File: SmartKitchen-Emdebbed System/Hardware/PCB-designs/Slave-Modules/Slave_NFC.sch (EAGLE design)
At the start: 29 parts, among them IC1 PCF8574T, IC2 7805DT, IC3 PCF8574T, IC4 74AHC1G126DBV, J1 RJ11-2L-B, J2 RJ11-2L-B, Q1 SPB80P06P, Q2 SPB80P06P, Q3 SPB80P06P

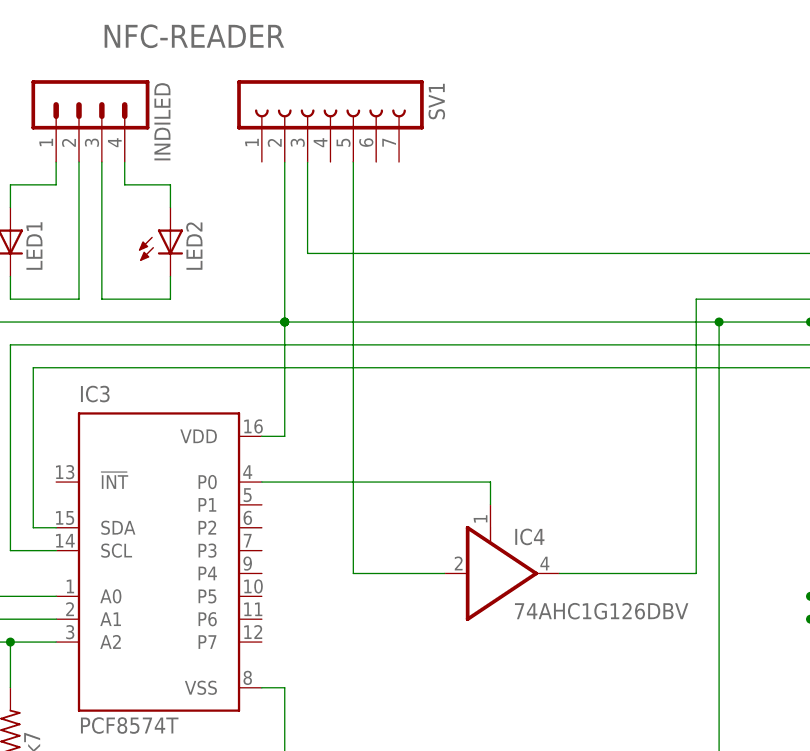
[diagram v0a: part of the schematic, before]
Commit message: Optimized PCB-board 2.0 with header for MAX232
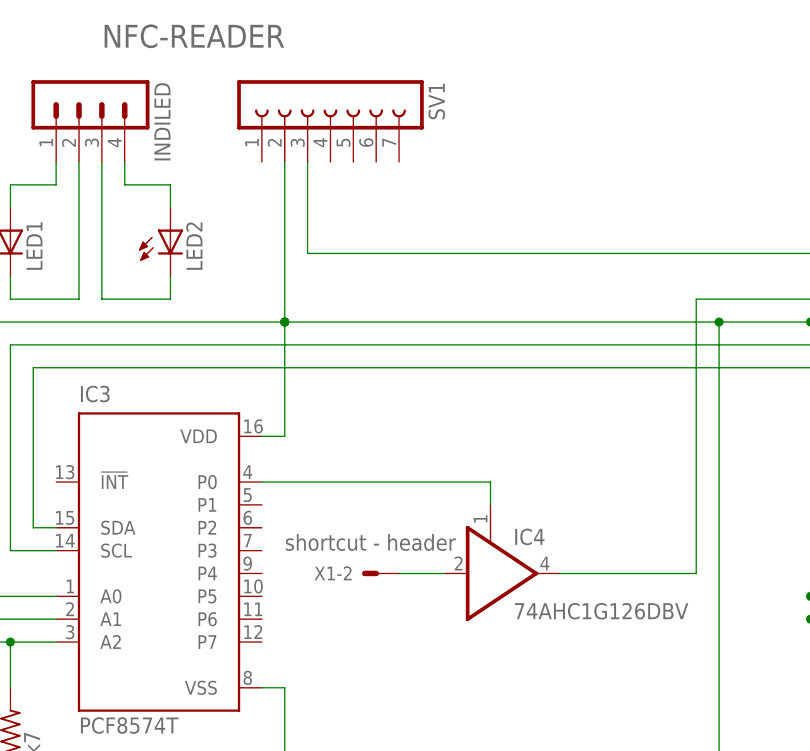
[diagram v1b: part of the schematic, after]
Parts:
- added X1: 22-23-2101, con-molex:22-23-2101
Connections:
- removed net N$27: IC4A.I, SV1.5
- new net N$26: IC4A.I, X1-2.S
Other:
- note added: "shortcut - header"
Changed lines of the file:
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@@
 <part name="U$1" library="Onboard_LEDstrip" deviceset="LED_S" device=""/>
 <part name="U$2" library="Onboard_LEDstrip" deviceset="LED_S" device=""/>
+<part name="X1" library="con-molex" deviceset="22-23-2101" device="">
+<attribute name="MPN" value="22-23-2101"/>
+<attribute name="OC_FARNELL" value="1756828"/>
+<attribute name="OC_NEWARK" value="94C0765"/>
+</part>
 </parts>
 <sheets>
@@
 <text x="292.1" y="142.24" size="2.54" layer="95">BUS-CONNECTION</text>
 <text x="309.88" y="73.66" size="2.54" layer="95">LEDSTRIPS</text>
+<text x="111.76" y="76.2" size="1.778" layer="95">shortcut - header</text>
 </plain>
 <instances>
@@
 <instance part="U$1" gate="LEDSTRIP" x="312.42" y="68.58" rot="R90"/>
 <instance part="U$2" gate="LEDSTRIP" x="330.2" y="68.58" rot="R90"/>
+<instance part="X1" gate="-2" x="121.92" y="73.66" rot="R180"/>
 </instances>
 <busses>
@@
 </segment>
 </net>
-<net name="N$27" class="0">
-<segment>
-<pinref part="SV1" gate="G$1" pin="5"/>
-<wire x1="119.38" y1="119.38" x2="119.38" y2="73.66" width="0.1524" layer="91"/>
-<pinref part="IC4" gate="A" pin="I"/>
-<wire x1="119.38" y1="73.66" x2="129.54" y2="73.66" width="0.1524" layer="91"/>
-</segment>
-</net>
 <net name="N$11" class="0">
 <segment>
@@
 </segment>
 </net>
+<net name="N$26" class="0">
+<segment>
+<pinref part="IC4" gate="A" pin="I"/>
+<pinref part="X1" gate="-2" pin="S"/>
+<wire x1="129.54" y1="73.66" x2="124.46" y2="73.66" width="0.1524" layer="91"/>
+</segment>
+</net>

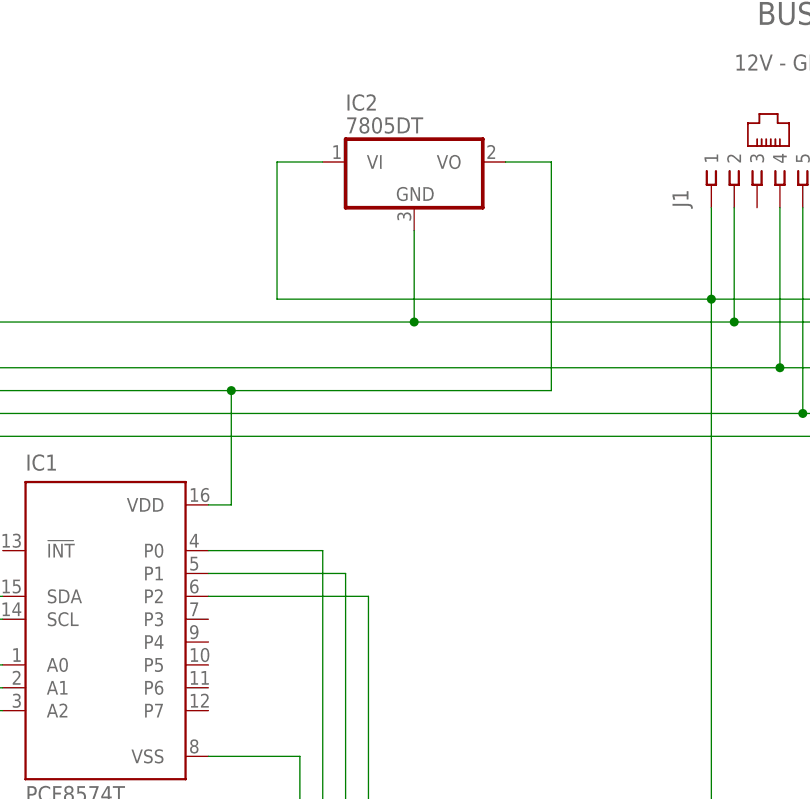
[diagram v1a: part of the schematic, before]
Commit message: Adding interference capacitors and testingcode
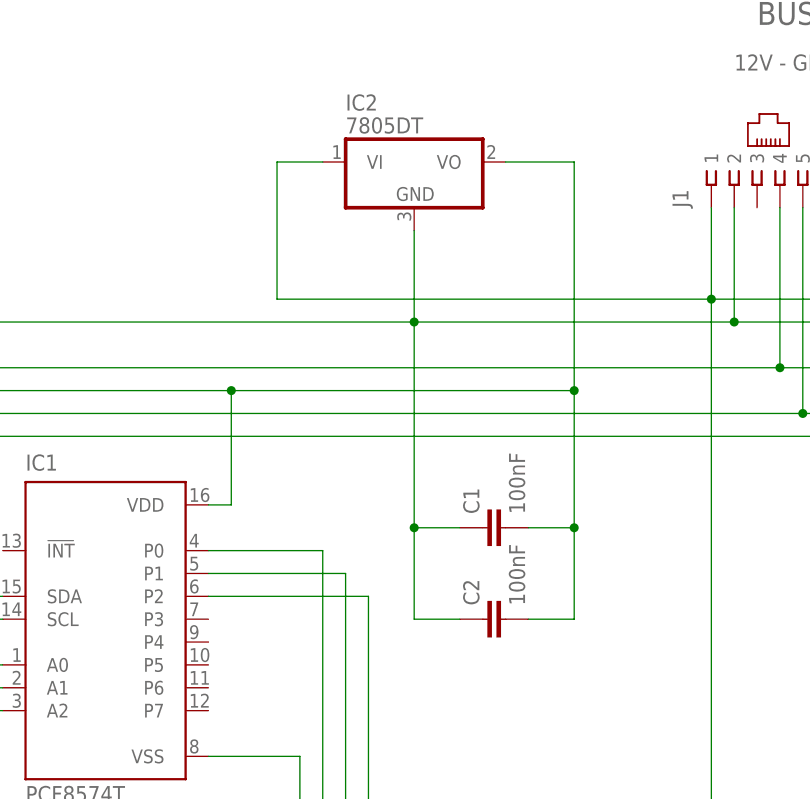
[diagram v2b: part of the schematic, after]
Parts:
- added C1, C2: 100nF, rcl:C-EUC0603
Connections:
- net AGND: now also C1.1, C2.1
- net N$21: now also C1.2, C2.2
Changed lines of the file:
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@@
 <attribute name="OC_NEWARK" value="94C0765"/>
 </part>
+<part name="C1" library="rcl" deviceset="C-EU" device="C0603" value="100nF"/>
+<part name="C2" library="rcl" deviceset="C-EU" device="C0603" value="100nF"/>
 </parts>
 <sheets>
@@
 <instance part="U$2" gate="LEDSTRIP" x="330.2" y="68.58" rot="R90"/>
 <instance part="X1" gate="-2" x="121.92" y="73.66" rot="R180"/>
+<instance part="C1" gate="G$1" x="261.62" y="86.36" rot="R90"/>
+<instance part="C2" gate="G$1" x="261.62" y="76.2" rot="R90"/>
 </instances>
 <busses>
@@
 <wire x1="114.3" y1="109.22" x2="254" y2="109.22" width="0.1524" layer="91"/>
 <junction x="254" y="109.22"/>
+<wire x1="254" y1="109.22" x2="254" y2="86.36" width="0.1524" layer="91"/>
+<pinref part="C1" gate="G$1" pin="1"/>
+<wire x1="254" y1="86.36" x2="259.08" y2="86.36" width="0.1524" layer="91"/>
+<pinref part="C2" gate="G$1" pin="1"/>
+<wire x1="259.08" y1="76.2" x2="254" y2="76.2" width="0.1524" layer="91"/>
+<wire x1="254" y1="76.2" x2="254" y2="86.36" width="0.1524" layer="91"/>
+<junction x="254" y="86.36"/>
 </segment>
 <segment>
@@
 <junction x="48.26" y="71.12"/>
 <pinref part="IC2" gate="A1" pin="VO"/>
-<wire x1="264.16" y1="127" x2="269.24" y2="127" width="0.1524" layer="91"/>
-<wire x1="269.24" y1="127" x2="269.24" y2="101.6" width="0.1524" layer="91"/>
-<wire x1="269.24" y1="101.6" x2="233.68" y2="101.6" width="0.1524" layer="91"/>
+<wire x1="264.16" y1="127" x2="271.78" y2="127" width="0.1524" layer="91"/>
+<wire x1="271.78" y1="127" x2="271.78" y2="101.6" width="0.1524" layer="91"/>
+<wire x1="271.78" y1="101.6" x2="233.68" y2="101.6" width="0.1524" layer="91"/>
 <wire x1="233.68" y1="101.6" x2="170.18" y2="101.6" width="0.1524" layer="91"/>
 <wire x1="170.18" y1="101.6" x2="170.18" y2="71.12" width="0.1524" layer="91"/>
@@
 <wire x1="111.76" y1="119.38" x2="111.76" y2="101.6" width="0.1524" layer="91"/>
 <junction x="111.76" y="101.6"/>
-</segment>
-</net>
+<pinref part="C1" gate="G$1" pin="2"/>
+<wire x1="266.7" y1="86.36" x2="271.78" y2="86.36" width="0.1524" layer="91"/>
+<wire x1="271.78" y1="86.36" x2="271.78" y2="101.6" width="0.1524" layer="91"/>
+<junction x="271.78" y="101.6"/>
+<pinref part="C2" gate="G$1" pin="2"/>
+<wire x1="266.7" y1="76.2" x2="271.78" y2="76.2" width="0.1524" layer="91"/>
+<wire x1="271.78" y1="76.2" x2="271.78" y2="86.36" width="0.1524" layer="91"/>
+<junction x="271.78" y="86.36"/>
+</segment>
+</net>

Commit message: fixing powerpeaks and nfc-read
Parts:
- added C3, C4: (no value), resistor:CPOL-EUB
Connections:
- net AGND: now also C3.-, C4.-
- net N$10: now also C3.+, C4.+, J1.3, J2.3
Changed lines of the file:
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@@
 <part name="C1" library="rcl" deviceset="C-EU" device="C0603" value="100nF"/>
 <part name="C2" library="rcl" deviceset="C-EU" device="C0603" value="100nF"/>
+<part name="C3" library="resistor" deviceset="CPOL-EU" device="B"/>
+<part name="C4" library="resistor" deviceset="CPOL-EU" device="B"/>
 </parts>
 <sheets>
@@
 <instance part="C1" gate="G$1" x="261.62" y="86.36" rot="R90"/>
 <instance part="C2" gate="G$1" x="261.62" y="76.2" rot="R90"/>
+<instance part="C3" gate="G$1" x="243.84" y="91.44" rot="R90"/>
+<instance part="C4" gate="G$1" x="243.84" y="86.36" rot="R90"/>
 </instances>
 <busses>
@@
 <wire x1="114.3" y1="109.22" x2="254" y2="109.22" width="0.1524" layer="91"/>
 <junction x="254" y="109.22"/>
-<wire x1="254" y1="109.22" x2="254" y2="86.36" width="0.1524" layer="91"/>
+<wire x1="254" y1="109.22" x2="254" y2="91.44" width="0.1524" layer="91"/>
 <pinref part="C1" gate="G$1" pin="1"/>
+<wire x1="254" y1="91.44" x2="254" y2="86.36" width="0.1524" layer="91"/>
 <wire x1="254" y1="86.36" x2="259.08" y2="86.36" width="0.1524" layer="91"/>
 <pinref part="C2" gate="G$1" pin="1"/>
@@
 <wire x1="254" y1="76.2" x2="254" y2="86.36" width="0.1524" layer="91"/>
 <junction x="254" y="86.36"/>
+<pinref part="C4" gate="G$1" pin="-"/>
+<wire x1="248.92" y1="86.36" x2="254" y2="86.36" width="0.1524" layer="91"/>
+<pinref part="C3" gate="G$1" pin="-"/>
+<wire x1="248.92" y1="91.44" x2="254" y2="91.44" width="0.1524" layer="91"/>
+<junction x="254" y="91.44"/>
 </segment>
 <segment>
@@
 <segment>
 <pinref part="J1" gate="G$1" pin="1"/>
-<wire x1="287.02" y1="121.92" x2="287.02" y2="111.76" width="0.1524" layer="91"/>
+<wire x1="287.02" y1="121.92" x2="287.02" y2="116.84" width="0.1524" layer="91"/>
+<wire x1="287.02" y1="116.84" x2="287.02" y2="111.76" width="0.1524" layer="91"/>
 <wire x1="287.02" y1="111.76" x2="287.02" y2="48.26" width="0.1524" layer="91"/>
 <wire x1="287.02" y1="48.26" x2="307.34" y2="48.26" width="0.1524" layer="91"/>
@@
 <pinref part="J2" gate="G$1" pin="1"/>
 <wire x1="307.34" y1="58.42" x2="307.34" y2="60.96" width="0.1524" layer="91"/>
-<wire x1="312.42" y1="121.92" x2="312.42" y2="111.76" width="0.1524" layer="91"/>
+<wire x1="312.42" y1="121.92" x2="312.42" y2="116.84" width="0.1524" layer="91"/>
+<wire x1="312.42" y1="116.84" x2="312.42" y2="111.76" width="0.1524" layer="91"/>
 <wire x1="312.42" y1="111.76" x2="287.02" y2="111.76" width="0.1524" layer="91"/>
 <junction x="287.02" y="111.76"/>
@@
 <wire x1="325.12" y1="58.42" x2="307.34" y2="58.42" width="0.1524" layer="91"/>
 <junction x="307.34" y="58.42"/>
+<pinref part="J1" gate="G$1" pin="3"/>
+<wire x1="292.1" y1="121.92" x2="292.1" y2="116.84" width="0.1524" layer="91"/>
+<wire x1="292.1" y1="116.84" x2="287.02" y2="116.84" width="0.1524" layer="91"/>
+<junction x="287.02" y="116.84"/>
+<pinref part="J2" gate="G$1" pin="3"/>
+<wire x1="317.5" y1="121.92" x2="317.5" y2="116.84" width="0.1524" layer="91"/>
+<wire x1="317.5" y1="116.84" x2="312.42" y2="116.84" width="0.1524" layer="91"/>
+<junction x="312.42" y="116.84"/>
+<pinref part="C3" gate="G$1" pin="+"/>
+<wire x1="241.3" y1="91.44" x2="238.76" y2="91.44" width="0.1524" layer="91"/>
+<wire x1="238.76" y1="91.44" x2="238.76" y2="111.76" width="0.1524" layer="91"/>
+<junction x="238.76" y="111.76"/>
+<pinref part="C4" gate="G$1" pin="+"/>
+<wire x1="241.3" y1="86.36" x2="238.76" y2="86.36" width="0.1524" layer="91"/>
+<wire x1="238.76" y1="86.36" x2="238.76" y2="91.44" width="0.1524" layer="91"/>
+<junction x="238.76" y="91.44"/>
 </segment>
 </net>
@@
 </sheet>
 </sheets>
+<errors>
+</errors>
 </schematic>
 </drawing>

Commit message: Final PCB-design for NFC-reader modules
I'm proud
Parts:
- C1, C2: value 100nF -> 4µ7; device rcl:C-EUC0603 -> resistor:CPOL-EUB
- C3, C4: value (none) -> 100n; device resistor:CPOL-EUB -> resistor:C-EUC0603
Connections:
- net AGND: now also C1.-, C2.-, C3.1, C4.1; no longer C1.1, C2.1, C3.-, C4.-
- net N$10: now also C1.+, C2.+; no longer C3.+, C4.+
- net N$21: now also C3.2, C4.2; no longer C1.2, C2.2
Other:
- moved on the sheet: IC2
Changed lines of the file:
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@@
 <attribute name="OC_NEWARK" value="94C0765"/>
 </part>
-<part name="C1" library="rcl" deviceset="C-EU" device="C0603" value="100nF"/>
-<part name="C2" library="rcl" deviceset="C-EU" device="C0603" value="100nF"/>
-<part name="C3" library="resistor" deviceset="CPOL-EU" device="B"/>
-<part name="C4" library="resistor" deviceset="CPOL-EU" device="B"/>
+<part name="C1" library="resistor" deviceset="CPOL-EU" device="B" value="4µ7"/>
+<part name="C2" library="resistor" deviceset="CPOL-EU" device="B" value="4µ7"/>
+<part name="C3" library="resistor" deviceset="C-EU" device="C0603" value="100n"/>
+<part name="C4" library="resistor" deviceset="C-EU" device="C0603" value="100n"/>
 </parts>
 <sheets>
@@
 <instance part="R9" gate="G$1" x="203.2" y="55.88" rot="R90"/>
 <instance part="AGND5" gate="VR1" x="195.58" y="43.18"/>
-<instance part="IC2" gate="A1" x="254" y="127"/>
+<instance part="IC2" gate="A1" x="254" y="129.54"/>
 <instance part="IC3" gate="G$1" x="96.52" y="76.2"/>
 <instance part="S2" gate="G$1" x="55.88" y="68.58" rot="R270"/>
@@
 <instance part="U$2" gate="LEDSTRIP" x="330.2" y="68.58" rot="R90"/>
 <instance part="X1" gate="-2" x="121.92" y="73.66" rot="R180"/>
-<instance part="C1" gate="G$1" x="261.62" y="86.36" rot="R90"/>
-<instance part="C2" gate="G$1" x="261.62" y="76.2" rot="R90"/>
-<instance part="C3" gate="G$1" x="243.84" y="91.44" rot="R90"/>
-<instance part="C4" gate="G$1" x="243.84" y="86.36" rot="R90"/>
+<instance part="C1" gate="G$1" x="243.84" y="116.84" rot="R90"/>
+<instance part="C2" gate="G$1" x="243.84" y="88.9" rot="R90"/>
+<instance part="C3" gate="G$1" x="261.62" y="116.84" rot="R90"/>
+<instance part="C4" gate="G$1" x="261.62" y="88.9" rot="R90"/>
 </instances>
 <busses>
@@
 <junction x="314.96" y="109.22"/>
 <pinref part="IC2" gate="A1" pin="GND"/>
-<wire x1="254" y1="119.38" x2="254" y2="109.22" width="0.1524" layer="91"/>
+<wire x1="254" y1="121.92" x2="254" y2="116.84" width="0.1524" layer="91"/>
+<wire x1="254" y1="116.84" x2="254" y2="109.22" width="0.1524" layer="91"/>
 <wire x1="254" y1="109.22" x2="289.56" y2="109.22" width="0.1524" layer="91"/>
 <junction x="289.56" y="109.22"/>
@@
 <wire x1="114.3" y1="109.22" x2="254" y2="109.22" width="0.1524" layer="91"/>
 <junction x="254" y="109.22"/>
-<wire x1="254" y1="109.22" x2="254" y2="91.44" width="0.1524" layer="91"/>
-<pinref part="C1" gate="G$1" pin="1"/>
-<wire x1="254" y1="91.44" x2="254" y2="86.36" width="0.1524" layer="91"/>
-<wire x1="254" y1="86.36" x2="259.08" y2="86.36" width="0.1524" layer="91"/>
-<pinref part="C2" gate="G$1" pin="1"/>
-<wire x1="259.08" y1="76.2" x2="254" y2="76.2" width="0.1524" layer="91"/>
-<wire x1="254" y1="76.2" x2="254" y2="86.36" width="0.1524" layer="91"/>
-<junction x="254" y="86.36"/>
-<pinref part="C4" gate="G$1" pin="-"/>
-<wire x1="248.92" y1="86.36" x2="254" y2="86.36" width="0.1524" layer="91"/>
-<pinref part="C3" gate="G$1" pin="-"/>
-<wire x1="248.92" y1="91.44" x2="254" y2="91.44" width="0.1524" layer="91"/>
-<junction x="254" y="91.44"/>
+<wire x1="254" y1="109.22" x2="254" y2="88.9" width="0.1524" layer="91"/>
+<pinref part="C4" gate="G$1" pin="1"/>
+<wire x1="254" y1="88.9" x2="259.08" y2="88.9" width="0.1524" layer="91"/>
+<pinref part="C2" gate="G$1" pin="-"/>
+<wire x1="248.92" y1="88.9" x2="254" y2="88.9" width="0.1524" layer="91"/>
+<junction x="254" y="88.9"/>
+<pinref part="C1" gate="G$1" pin="-"/>
+<wire x1="248.92" y1="116.84" x2="254" y2="116.84" width="0.1524" layer="91"/>
+<junction x="254" y="116.84"/>
+<pinref part="C3" gate="G$1" pin="1"/>
+<wire x1="259.08" y1="116.84" x2="254" y2="116.84" width="0.1524" layer="91"/>
 </segment>
 <segment>
@@
 <junction x="287.02" y="111.76"/>
 <pinref part="IC2" gate="A1" pin="VI"/>
-<wire x1="243.84" y1="127" x2="238.76" y2="127" width="0.1524" layer="91"/>
-<wire x1="238.76" y1="127" x2="238.76" y2="111.76" width="0.1524" layer="91"/>
-<wire x1="238.76" y1="111.76" x2="287.02" y2="111.76" width="0.1524" layer="91"/>
+<wire x1="243.84" y1="129.54" x2="236.22" y2="129.54" width="0.1524" layer="91"/>
+<wire x1="236.22" y1="129.54" x2="236.22" y2="116.84" width="0.1524" layer="91"/>
+<wire x1="236.22" y1="116.84" x2="236.22" y2="111.76" width="0.1524" layer="91"/>
+<wire x1="236.22" y1="111.76" x2="287.02" y2="111.76" width="0.1524" layer="91"/>
 <pinref part="U$1" gate="LEDSTRIP" pin="+"/>
 <pinref part="U$2" gate="LEDSTRIP" pin="+"/>
@@
 <wire x1="325.12" y1="58.42" x2="307.34" y2="58.42" width="0.1524" layer="91"/>
 <junction x="307.34" y="58.42"/>
+<pinref part="C2" gate="G$1" pin="+"/>
+<wire x1="241.3" y1="88.9" x2="236.22" y2="88.9" width="0.1524" layer="91"/>
+<junction x="236.22" y="111.76"/>
+<wire x1="236.22" y1="88.9" x2="236.22" y2="111.76" width="0.1524" layer="91"/>
+<pinref part="C1" gate="G$1" pin="+"/>
+<wire x1="241.3" y1="116.84" x2="236.22" y2="116.84" width="0.1524" layer="91"/>
+<junction x="236.22" y="116.84"/>
 <pinref part="J1" gate="G$1" pin="3"/>
 <wire x1="292.1" y1="121.92" x2="292.1" y2="116.84" width="0.1524" layer="91"/>
@@
 <wire x1="317.5" y1="116.84" x2="312.42" y2="116.84" width="0.1524" layer="91"/>
 <junction x="312.42" y="116.84"/>
-<pinref part="C3" gate="G$1" pin="+"/>
-<wire x1="241.3" y1="91.44" x2="238.76" y2="91.44" width="0.1524" layer="91"/>
-<wire x1="238.76" y1="91.44" x2="238.76" y2="111.76" width="0.1524" layer="91"/>
-<junction x="238.76" y="111.76"/>
-<pinref part="C4" gate="G$1" pin="+"/>
-<wire x1="241.3" y1="86.36" x2="238.76" y2="86.36" width="0.1524" layer="91"/>
-<wire x1="238.76" y1="86.36" x2="238.76" y2="91.44" width="0.1524" layer="91"/>
-<junction x="238.76" y="91.44"/>
 </segment>
 </net>
@@
 <junction x="48.26" y="71.12"/>
 <pinref part="IC2" gate="A1" pin="VO"/>
-<wire x1="264.16" y1="127" x2="271.78" y2="127" width="0.1524" layer="91"/>
-<wire x1="271.78" y1="127" x2="271.78" y2="101.6" width="0.1524" layer="91"/>
+<wire x1="264.16" y1="129.54" x2="271.78" y2="129.54" width="0.1524" layer="91"/>
+<wire x1="271.78" y1="129.54" x2="271.78" y2="116.84" width="0.1524" layer="91"/>
+<wire x1="271.78" y1="116.84" x2="271.78" y2="101.6" width="0.1524" layer="91"/>
 <wire x1="271.78" y1="101.6" x2="233.68" y2="101.6" width="0.1524" layer="91"/>
 <wire x1="233.68" y1="101.6" x2="170.18" y2="101.6" width="0.1524" layer="91"/>
@@
 <wire x1="111.76" y1="119.38" x2="111.76" y2="101.6" width="0.1524" layer="91"/>
 <junction x="111.76" y="101.6"/>
-<pinref part="C1" gate="G$1" pin="2"/>
-<wire x1="266.7" y1="86.36" x2="271.78" y2="86.36" width="0.1524" layer="91"/>
-<wire x1="271.78" y1="86.36" x2="271.78" y2="101.6" width="0.1524" layer="91"/>
+<wire x1="271.78" y1="88.9" x2="271.78" y2="101.6" width="0.1524" layer="91"/>
 <junction x="271.78" y="101.6"/>
-<pinref part="C2" gate="G$1" pin="2"/>
-<wire x1="266.7" y1="76.2" x2="271.78" y2="76.2" width="0.1524" layer="91"/>
-<wire x1="271.78" y1="76.2" x2="271.78" y2="86.36" width="0.1524" layer="91"/>
-<junction x="271.78" y="86.36"/>
+<pinref part="C4" gate="G$1" pin="2"/>
+<wire x1="266.7" y1="88.9" x2="271.78" y2="88.9" width="0.1524" layer="91"/>
+<pinref part="C3" gate="G$1" pin="2"/>
+<wire x1="266.7" y1="116.84" x2="271.78" y2="116.84" width="0.1524" layer="91"/>
+<junction x="271.78" y="116.84"/>
 </segment>
 </net>
@@
 </sheet>
 </sheets>
-<errors>
-</errors>
 </schematic>
 </drawing>
